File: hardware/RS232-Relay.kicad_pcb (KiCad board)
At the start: 2 copper layers, 82.5 x 151 mm, 204 parts, among them J1 Conn_01x08, J2 Conn_01x02, J3 Conn_01x08, J4 Conn_01x09, J5 Conn_01x09, J6 Conn_01x08, J7 RS232_1, J8 RS232_2, K1 G5V-1, K13 G5V-1, K14 G5V-1, K15 G5V-1, K2 G5V-1, K3 G5V-1, K4 G5V-1, K5 G5V-1, K6 G5V-1, K7 G5V-1, K8 G5V-1, K9 G5V-1, Q1 SS8050, Q10 SS8050, Q11 SS8050, Q12 SS8050, Q13 SS8050, Q14 SS8050, Q15 SS8050, Q16 SS8050, Q17 SS8050, Q18 SS8050, Q19 SS8050, Q2 SS8050, Q20 SS8050, Q21 SS8050, Q22 SS8050, Q23 SS8050, Q24 SS8050, Q3 SS8050, Q4 SS8050, Q5 SS8050, Q6 SS8050, Q7 SS8050, Q8 SS8050, Q9 SS8050, SW2 SW_SPST, SW3 SW_SPST, U1 TEC2-1210WI, U10 PC817, U11 PC817, U12 PC817, U13 PC817, U14 PC817, U15 PC817, U2 PC817, U3 PCF8575DBR, U4 MAX3232, U5 PC817, U6 PC817, U7 PC817, U8 PC817, U9 PC817

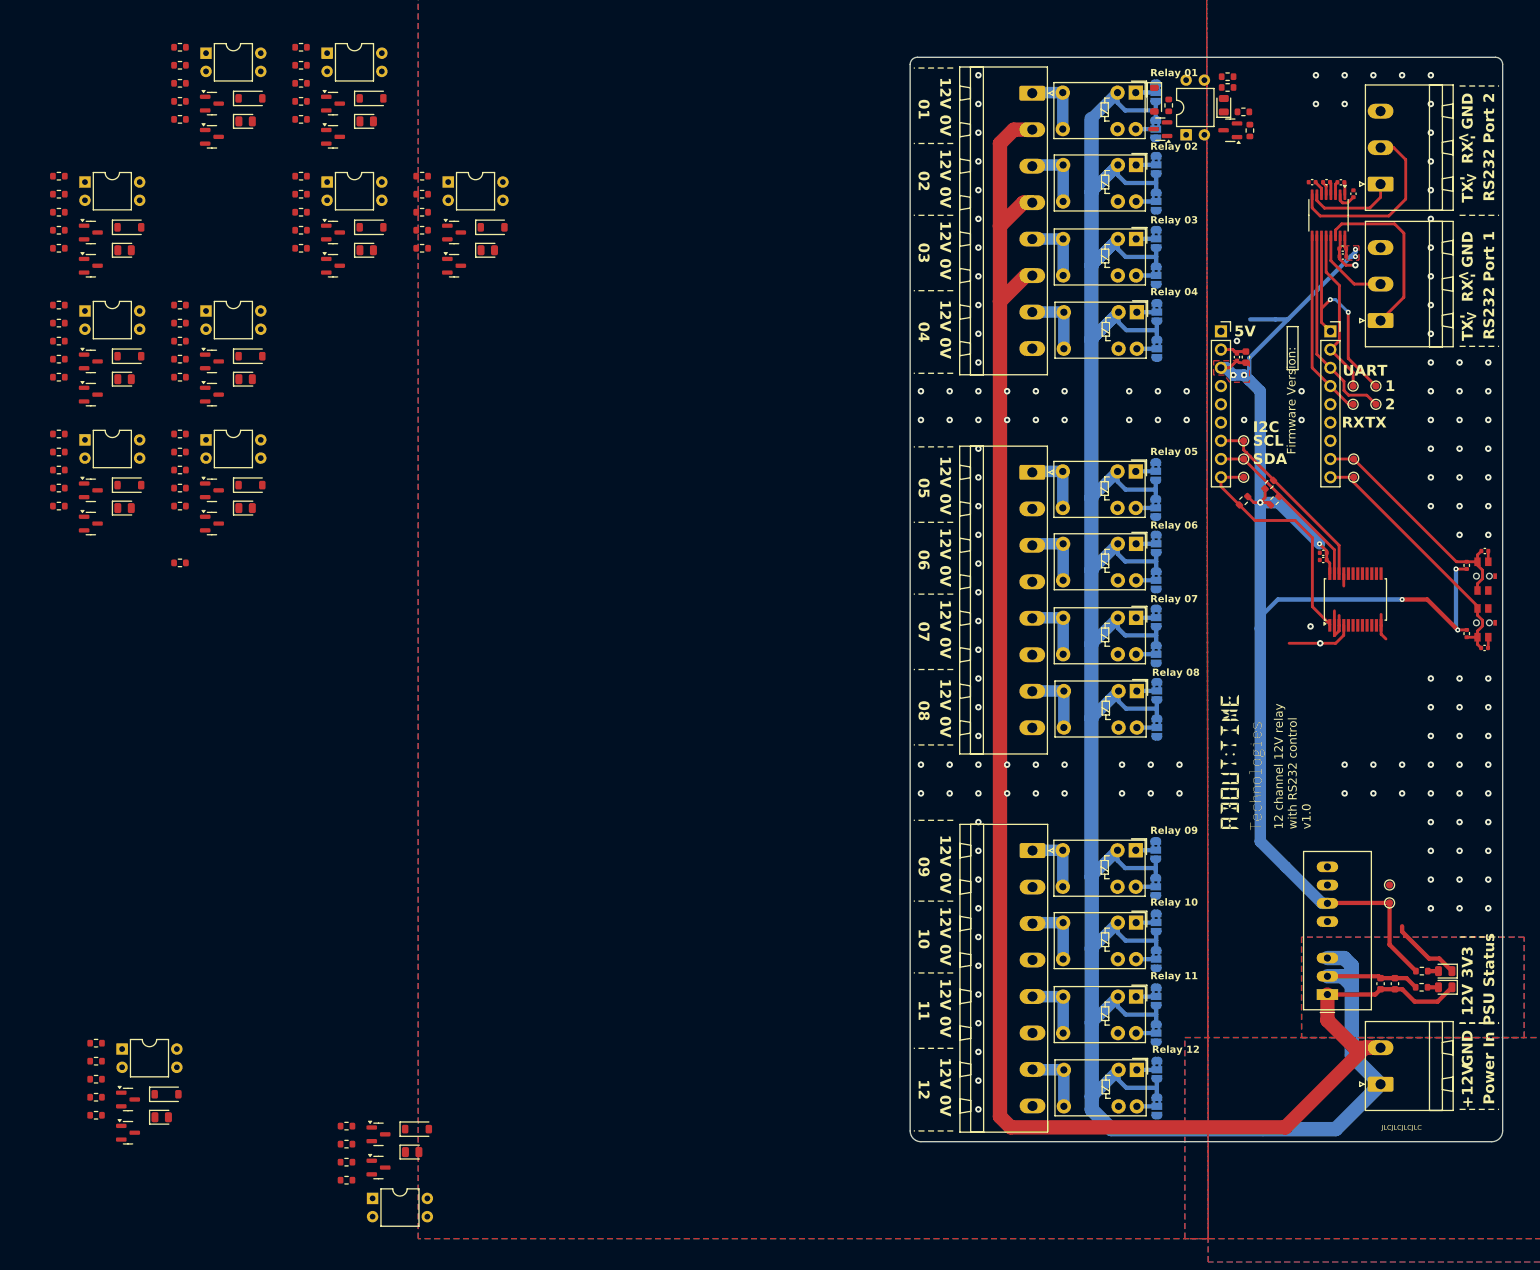
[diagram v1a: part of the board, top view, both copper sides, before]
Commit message: It could work but it's too big
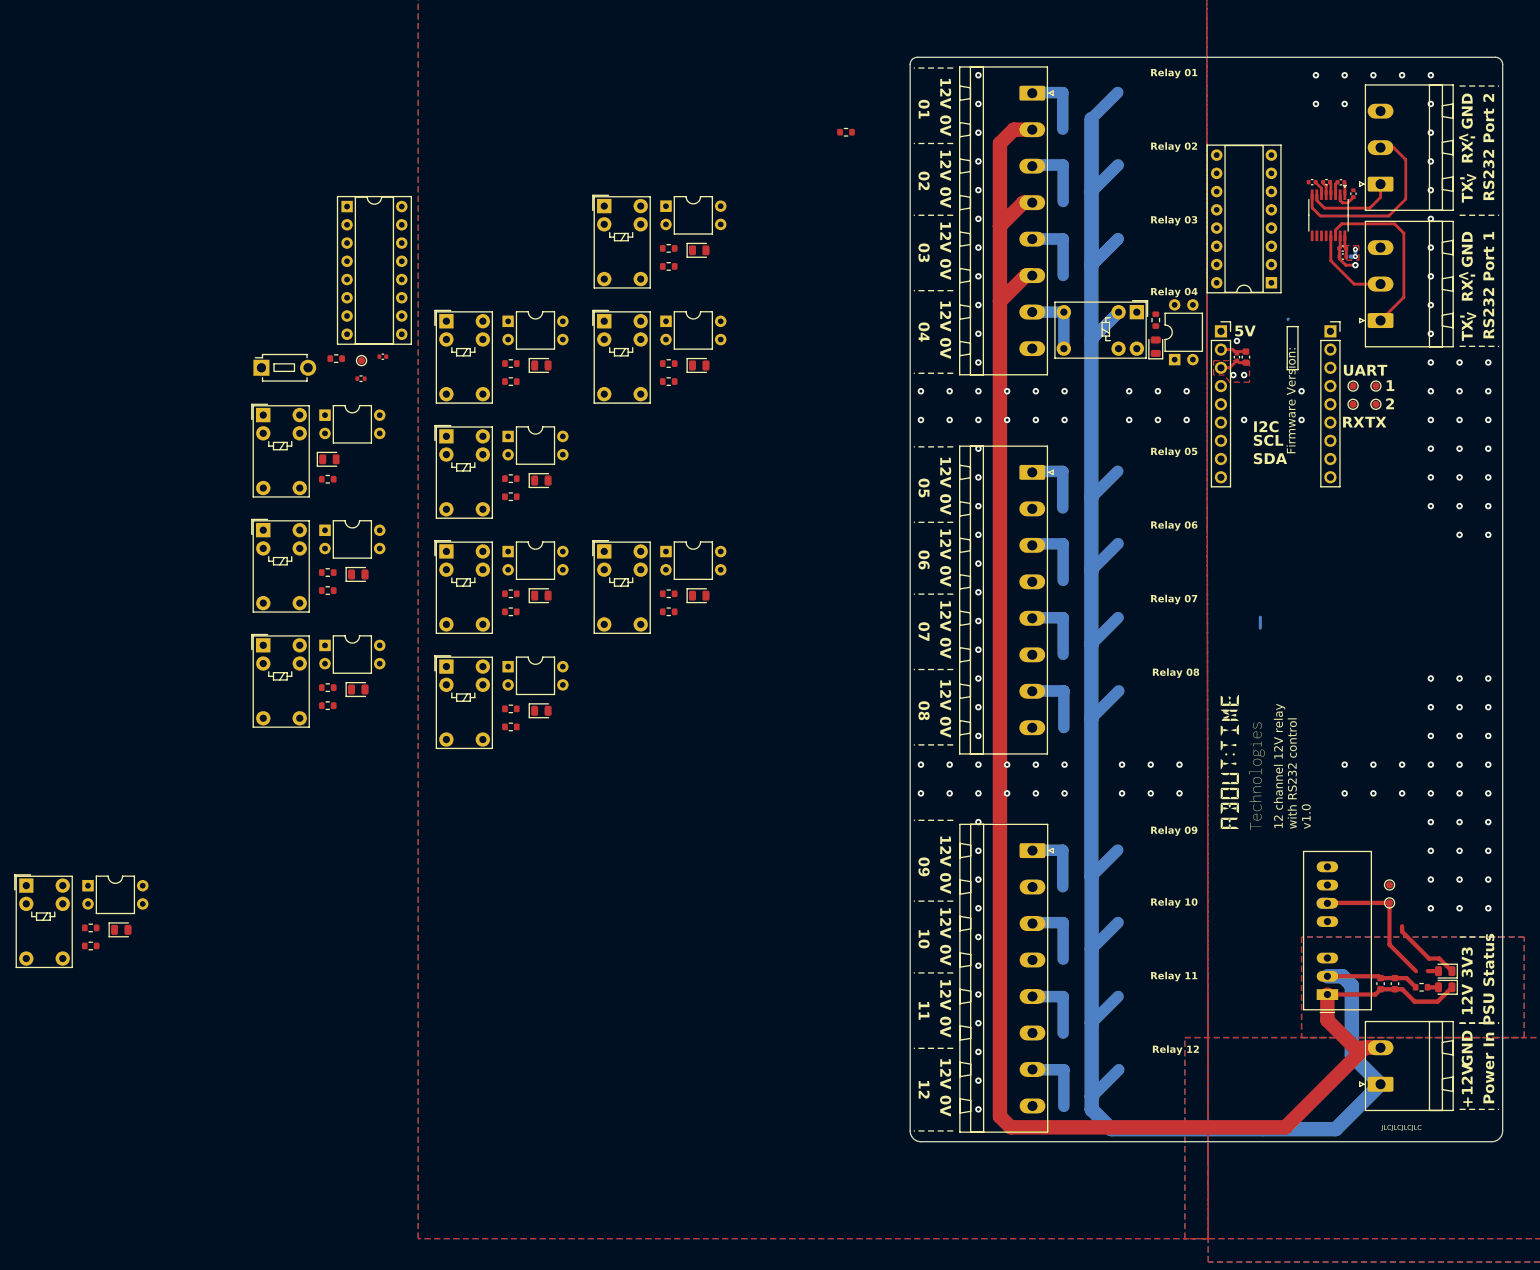
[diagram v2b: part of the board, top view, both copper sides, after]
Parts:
- removed C12, C15: 1uF, Capacitor_SMD:C_0402_1005Metric
- removed C13: 0.1uF, Capacitor_SMD:C_0402_1005Metric
- removed D15, D17, D19, D21, D29, D31, D33: 1N4148W, Diode_SMD:D_SOD-123
- removed D16, D18, D20, D22, D23: RED, LED_SMD:LED_0805_2012Metric
- removed JP1, JP10, JP11, JP12, JP2, JP3, JP4, JP49, JP5, JP50, JP51, JP52, JP53, JP54, JP55, JP56, JP57, JP58, JP59, JP6, JP60, JP7, JP8, JP9: Jumper_3_Bridged12, Jumper:SolderJumper-3_P1.3mm_Bridged2Bar12_RoundedPad1.0x1.5mm
- removed K13, K14, K15: G5V-1, Relay_THT:Relay_SPDT_Omron_G5V-1
- removed Q1, Q10, Q11, Q12, Q13, Q14, Q15, Q16, Q17, Q18, Q19, Q2, Q20, Q21, Q22, Q23, Q24, Q3, Q4, Q5, Q6, Q7, Q8, Q9: SS8050, Package_TO_SOT_SMD:SOT-23
- removed R10: 2000R, Resistor_SMD:R_0603_1608Metric
- removed R29, R30, R31, R32, R33, R34, R35, R36, R37, R38, R39, R40, R41, R42, R43, R44, R45, R46, R47, R48, R49, R50, R51, R52, R53, R54, R55: 4.7kR, Resistor_SMD:R_0603_1608Metric
- removed R56, R57, R58, R59, R60, R61, R62, R63, R64, R65, R66, R67: 100kR, Resistor_SMD:R_0603_1608Metric
- removed R7: 10K, Resistor_SMD:R_0402_1005Metric
- removed SW3: SW_SPST, Switch:PTS841
- removed TP10: I2C_SCL, TestPoint:TestPoint_Pad_D1.0mm
- removed TP11: I2C_INT, TestPoint:TestPoint_Pad_D1.0mm
- removed TP13: BTN_02, TestPoint:TestPoint_Pad_D1.0mm
- removed TP9: I2C_SDA, TestPoint:TestPoint_Pad_D1.0mm
- added K10: G5V-1, Relay_THT:Relay_SPDT_Omron_G5V-1, F.Cu at (3.92, 88.3)
- added K11: G5V-1, Relay_THT:Relay_SPDT_Omron_G5V-1, F.Cu at (3.92, 120.3)
- added K12: G5V-1, Relay_THT:Relay_SPDT_Omron_G5V-1, F.Cu at (100.1, 71.0)
- added U16: ULN2003, Package_DIP:DIP-16_W7.62mm_Socket, F.Cu at (-9.91, 56.3)
- D11, D13, D2, D4, D9: value 1N4148W -> RED; footprint Diode_SMD:D_SOD-123 -> LED_SMD:LED_0805_2012Metric
- J1, J3, J6: footprint Header:PhoenixContact_MSTBA_2,5_8-G-5,08_1x08_P5.08mm_Horizontal -> Connector_Phoenix_MSTB:PhoenixContact_MSTBA_2,5_8-G-5,08_1x08_P5.08mm_Horizontal
- R1: value 1000R -> 2000R
- R11, R15, R17, R21, R23, R3: value 2000R -> 220R
- R13, R19, R25, R27: value 4.7kR -> 220R
- R16, R22, R26, R28, R5: value 4.7kR -> 2000R
- R2: value 1000R -> 220R
- R4, R9: value 4K7 -> 220R
- R8: value 4K7 -> 2000R
- SW2: footprint Switch:PTS841 -> Button_Switch_THT:SW_PUSH_1P1T_6x3.5mm_H4.3_APEM_MJTP1243
- U3: value PCF8575DBR -> ULN2003; footprint Package_SO:SSOP-24_5.3x8.2mm_P0.65mm -> Package_DIP:DIP-16_W7.62mm_Socket
- moved SW2 172.5 mm to (-21.8, 78.7), turned to 0 degrees
- moved R27 157.1 mm to (59.6, 45.9)
- moved R6 156.1 mm to (-7.96, 80.3), turned to 0 degrees
- moved C14 155.8 mm to (-4.93, 77.2), turned to 0 degrees
- moved K5 155.3 mm to (-54.6, 150.8), turned to 0 degrees
- moved R28 153.7 mm to (102.7, 72.1), turned to -90 degrees
- moved D14 144.2 mm to (102.7, 75.8), turned to 90 degrees
- moved K8 143.0 mm to (-21.6, 101.3), turned to 0 degrees
- moved K2 140.6 mm to (-21.6, 85.3), turned to 0 degrees
- moved TP12 138.8 mm to (-7.89, 77.7)
- moved K1 138.7 mm to (-21.6, 117.4), turned to 0 degrees
- moved U15 135.0 mm to (105.3, 77.6), turned to 90 degrees
- moved R8 134.9 mm to (-12.6, 125.8), turned to 0 degrees
- moved R26 134.8 mm to (12.9, 128.7), turned to 0 degrees
- moved R4 134.1 mm to (-12.6, 123.3), turned to 0 degrees
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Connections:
- net /Relay-Module2/RELAY_OUT_03 renamed /RELAY_OUT_11
- D1 pad 1: Net-(D1-K) -> /ULN_RELAY_05
- D10 pad 1: Net-(D10-K) -> /ULN_RELAY_12
- D11 pad 1: +12V -> /ULN_RELAY_01
- D12 pad 1: Net-(D12-K) -> /ULN_RELAY_02
- D13 pad 1: +12V -> /ULN_RELAY_03
- D14 pad 1: Net-(D14-K) -> /ULN_RELAY_04
- D2 pad 1: +12V -> /ULN_RELAY_06
- D3 pad 1: Net-(D3-K) -> /ULN_RELAY_07
- D4 pad 1: +12V -> /ULN_RELAY_08
- D7 pad 1: Net-(D7-K) -> /ULN_RELAY_09
- D8 pad 1: Net-(D8-K) -> /ULN_RELAY_10
- D9 pad 1: +12V -> /ULN_RELAY_11
- J1 pad 1: /Relay-Module/RELAY_OUT_01 -> /RELAY_OUT_01
- J1 pad 2: GNDREF -> GND
- J1 pad 3: /Relay-Module/RELAY_OUT_02 -> /RELAY_OUT_02
- J1 pad 4: GNDREF -> GND
- J1 pad 5: /Relay-Module/RELAY_OUT_03 -> /RELAY_OUT_03
- J1 pad 6: GNDREF -> GND
- J1 pad 7: /Relay-Module/RELAY_OUT_04 -> /RELAY_OUT_04
- J1 pad 8: GNDREF -> GND
- J3 pad 1: /Relay-Module1/RELAY_OUT_01 -> /RELAY_OUT_05
- J3 pad 2: GNDREF -> GND
- J3 pad 3: /Relay-Module1/RELAY_OUT_02 -> /RELAY_OUT_06
- J3 pad 4: GNDREF -> GND
- J3 pad 5: /Relay-Module1/RELAY_OUT_03 -> /RELAY_OUT_07
- J3 pad 6: GNDREF -> GND
- J3 pad 7: /Relay-Module1/RELAY_OUT_04 -> /RELAY_OUT_08
- J3 pad 8: GNDREF -> GND
- J4 pad 7: I2C_SCL -> /ESP_32_GPIO_03
- J4 pad 8: I2C_SDA -> /ESP_32_GPIO_04
- J4 pad 9: I2C_INT -> /ESP_32_GPIO_05
- J5 pad 3: UART_2_TX -> BTN_01
- J5 pad 4: UART_2_RX -> /ESP_32_GPIO_15
- J5 pad 8: BTN_01 -> /ESP_32_GPIO_21
- J5 pad 9: BTN_02 -> /ESP_32_GPIO_22
- J6 pad 1: /Relay-Module2/RELAY_OUT_01 -> /RELAY_OUT_09
- J6 pad 2: GNDREF -> GND
- J6 pad 3: /Relay-Module2/RELAY_OUT_02 -> /RELAY_OUT_10
- J6 pad 4: GNDREF -> GND
- J6 pad 6: GNDREF -> GND
- J6 pad 7: /Relay-Module2/RELAY_OUT_04 -> /RELAY_OUT_12
- J6 pad 8: GNDREF -> GND
- K1 pad 1: /Relay-Module/Relay-NO-ISO1/RELAY_OFF -> GND
- K1 pad 10: /Relay-Module/Relay-NO-ISO1/RELAY_ON -> +12V
- K1 pad 5: /Relay-Module/RELAY_OUT_02 -> /RELAY_OUT_06
- K1 pad 6: /Relay-Module/RELAY_OUT_02 -> /RELAY_OUT_06
- K1 pad 9: Net-(D2-A) -> /ULN_RELAY_06
- K2 pad 1: /Relay-Module1/Relay-NO-ISO1/RELAY_OFF -> GND
- K2 pad 10: /Relay-Module1/Relay-NO-ISO1/RELAY_ON -> +12V
- K2 pad 5: /Relay-Module1/RELAY_OUT_02 -> /RELAY_OUT_07
- K2 pad 6: /Relay-Module1/RELAY_OUT_02 -> /RELAY_OUT_07
- K2 pad 9: Net-(D4-A) -> /ULN_RELAY_07
- K3 pad 1: /Relay-Module2/Relay-NO-ISO1/RELAY_OFF -> GND
- K3 pad 10: /Relay-Module2/Relay-NO-ISO1/RELAY_ON -> +12V
- K3 pad 5: /Relay-Module2/RELAY_OUT_02 -> /RELAY_OUT_08
- K3 pad 6: /Relay-Module2/RELAY_OUT_02 -> /RELAY_OUT_08
- K3 pad 9: Net-(D9-A) -> /ULN_RELAY_08
- K4 pad 1: /Relay-Module/Relay-NO-ISO2/RELAY_OFF -> GND
- K4 pad 10: /Relay-Module/Relay-NO-ISO2/RELAY_ON -> +12V
- K4 pad 5: /Relay-Module/RELAY_OUT_03 -> /RELAY_OUT_09
- K4 pad 6: /Relay-Module/RELAY_OUT_03 -> /RELAY_OUT_09
- K4 pad 9: Net-(D11-A) -> /ULN_RELAY_09
- K5 pad 1: /Relay-Module1/Relay-NO-ISO2/RELAY_OFF -> GND
- K5 pad 10: /Relay-Module1/Relay-NO-ISO2/RELAY_ON -> +12V
- K5 pad 5: /Relay-Module1/RELAY_OUT_03 -> /RELAY_OUT_10
- K5 pad 6: /Relay-Module1/RELAY_OUT_03 -> /RELAY_OUT_10
- K5 pad 9: Net-(D13-A) -> /ULN_RELAY_10
- K6 pad 1: /Relay-Module2/Relay-NO-ISO2/RELAY_OFF -> GND
- K6 pad 10: /Relay-Module2/Relay-NO-ISO2/RELAY_ON -> +12V
- K6 pad 9: Net-(D15-A) -> /ULN_RELAY_11
- K7 pad 1: /Relay-Module/Relay-NO-ISO3/RELAY_OFF -> GND
- K7 pad 10: /Relay-Module/Relay-NO-ISO3/RELAY_ON -> +12V
- K7 pad 5: /Relay-Module/RELAY_OUT_04 -> /RELAY_OUT_12
- K7 pad 6: /Relay-Module/RELAY_OUT_04 -> /RELAY_OUT_12
- K7 pad 9: Net-(D17-A) -> /ULN_RELAY_12
- K8 pad 1: /Relay-Module1/Relay-NO-ISO3/RELAY_OFF -> GND
- K8 pad 10: /Relay-Module1/Relay-NO-ISO3/RELAY_ON -> +12V
- K8 pad 5: /Relay-Module1/RELAY_OUT_04 -> /RELAY_OUT_01
- K8 pad 6: /Relay-Module1/RELAY_OUT_04 -> /RELAY_OUT_01
- K8 pad 9: Net-(D19-A) -> /ULN_RELAY_01
- K9 pad 1: /Relay-Module2/Relay-NO-ISO3/RELAY_OFF -> GND
- K9 pad 10: /Relay-Module2/Relay-NO-ISO3/RELAY_ON -> +12V
- K9 pad 5: /Relay-Module2/RELAY_OUT_04 -> /RELAY_OUT_02
- K9 pad 6: /Relay-Module2/RELAY_OUT_04 -> /RELAY_OUT_02
- K9 pad 9: Net-(D21-A) -> /ULN_RELAY_02
- R11 pad 1: +3V3 -> /RELAY_IN_08
- R11 pad 2: Net-(D7-A) -> Net-(R11-Pad2)
- R12 pad 1: +3V3 -> +12V
- R12 pad 2: Net-(D8-A) -> Net-(D4-A)
- R13 pad 1: Net-(R13-Pad1) -> /RELAY_IN_09
- R13 pad 2: Net-(Q11-B) -> Net-(R13-Pad2)
- R14 pad 1: +3V3 -> +12V
- R14 pad 2: Net-(D10-A) -> Net-(D7-A)
- R15 pad 1: +3V3 -> /RELAY_IN_10
- R15 pad 2: Net-(D12-A) -> Net-(R15-Pad2)
- R16 pad 1: Net-(R16-Pad1) -> +12V
- R16 pad 2: Net-(Q12-B) -> Net-(D8-A)
- R17 pad 1: +3V3 -> /RELAY_IN_11
- R17 pad 2: Net-(D14-A) -> Net-(R17-Pad2)
- R18 pad 1: +3V3 -> +12V
- R18 pad 2: Net-(D16-A) -> Net-(D9-A)
- R19 pad 1: Net-(R19-Pad1) -> /RELAY_IN_12
- R19 pad 2: Net-(Q16-B) -> Net-(R19-Pad2)
- R20 pad 1: +3V3 -> +12V
- R20 pad 2: Net-(D18-A) -> Net-(D10-A)
- R21 pad 1: +3V3 -> /RELAY_IN_01
- R21 pad 2: Net-(D20-A) -> Net-(R21-Pad2)
- R22 pad 1: Net-(R22-Pad1) -> +12V
- R22 pad 2: Net-(Q17-B) -> Net-(D11-A)
- R23 pad 1: +3V3 -> /RELAY_IN_02
- R23 pad 2: Net-(D22-A) -> Net-(R23-Pad2)
- R24 pad 1: +3V3 -> +12V
- R24 pad 2: Net-(D23-A) -> Net-(D12-A)
- R25 pad 1: Net-(R25-Pad1) -> /RELAY_IN_03
- R25 pad 2: Net-(Q18-B) -> Net-(R25-Pad2)
- R26 pad 1: +3V3 -> +12V
- R26 pad 2: Net-(R26-Pad2) -> Net-(D13-A)
- R27 pad 1: +3V3 -> /RELAY_IN_04
- R28 pad 1: Net-(R28-Pad1) -> +12V
- R28 pad 2: Net-(Q19-B) -> Net-(D14-A)
- R3 pad 1: +3V3 -> /RELAY_IN_05
- R3 pad 2: Net-(D1-A) -> Net-(R3-Pad2)
- R4 pad 1: I2C_SCL -> /RELAY_IN_06
- R4 pad 2: +3V3 -> Net-(R4-Pad2)
- R5 pad 1: Net-(R5-Pad1) -> +12V
- R5 pad 2: Net-(Q10-B) -> Net-(D1-A)
- R8 pad 1: +3V3 -> +12V
- R8 pad 2: I2C_SDA -> Net-(D2-A)
- R9 pad 1: I2C_INT -> /RELAY_IN_07
- R9 pad 2: +3V3 -> Net-(R9-Pad2)
- U1 pad 3: +12V -> GND
- U10 pad 1: Net-(R35-Pad2) -> Net-(R17-Pad2)
- U10 pad 2: Net-(D14-K) -> GNDREF
- U10 pad 3: Net-(R28-Pad1) -> /ULN_ISO_11
- U11 pad 1: Net-(R36-Pad2) -> Net-(R19-Pad2)
- U11 pad 2: Net-(D16-K) -> GNDREF
- U11 pad 3: Net-(R31-Pad1) -> /ULN_ISO_12
- U12 pad 1: Net-(R37-Pad2) -> Net-(R21-Pad2)
- U12 pad 2: Net-(D18-K) -> GNDREF
- U12 pad 3: Net-(R34-Pad1) -> /ULN_ISO_01
- U13 pad 1: Net-(R38-Pad2) -> Net-(R23-Pad2)
- U13 pad 2: Net-(D20-K) -> GNDREF
- U13 pad 3: Net-(R46-Pad1) -> /ULN_ISO_02
- U14 pad 1: Net-(R39-Pad2) -> Net-(R25-Pad2)
- U14 pad 2: Net-(D22-K) -> GNDREF
- U14 pad 3: Net-(R49-Pad1) -> /ULN_ISO_03
- U15 pad 1: Net-(R40-Pad2) -> Net-(R27-Pad2)
- U15 pad 2: Net-(D23-K) -> GNDREF
- U15 pad 3: Net-(R52-Pad1) -> /ULN_ISO_04
- U2 pad 1: Net-(R26-Pad2) -> Net-(R3-Pad2)
- U2 pad 2: Net-(D1-K) -> GNDREF
- U2 pad 3: Net-(R5-Pad1) -> /ULN_ISO_05
- U3 pad 1: I2C_INT -> /ULN_ISO_01
- U3 pad 10: RELAY_IN_06 -> unconnected-(U3-O7-Pad10)
- U3 pad 11: RELAY_IN_05 -> /ULN_RELAY_06
- U3 pad 12: GNDREF -> /ULN_RELAY_05
- U3 pad 13: RELAY_IN_04 -> /ULN_RELAY_04
- U3 pad 14: RELAY_IN_03 -> /ULN_RELAY_03
- U3 pad 15: RELAY_IN_02 -> /ULN_RELAY_02
- U3 pad 16: RELAY_IN_01 -> /ULN_RELAY_01
- U3 pad 2: GNDREF -> /ULN_ISO_02
- U3 pad 3: GNDREF -> /ULN_ISO_03
- U3 pad 4: RELAY_IN_12 -> /ULN_ISO_04
- U3 pad 5: RELAY_IN_11 -> /ULN_ISO_05
- U3 pad 6: RELAY_IN_10 -> /ULN_ISO_06
- U3 pad 7: RELAY_IN_09 -> unconnected-(U3-I7-Pad7)
- U3 pad 8: RELAY_IN_08 -> GND
- U3 pad 9: RELAY_IN_07 -> +12V
- U5 pad 1: Net-(R27-Pad2) -> Net-(R4-Pad2)
- U5 pad 2: Net-(D3-K) -> GNDREF
- U5 pad 3: Net-(R13-Pad1) -> /ULN_ISO_06
- U6 pad 1: Net-(R29-Pad2) -> Net-(R9-Pad2)
- U6 pad 2: Net-(D7-K) -> GNDREF
- U6 pad 3: Net-(R16-Pad1) -> /ULN_ISO_07
- U7 pad 1: Net-(R30-Pad2) -> Net-(R11-Pad2)
- U7 pad 2: Net-(D8-K) -> GNDREF
- U7 pad 3: Net-(R19-Pad1) -> /ULN_ISO_08
- U8 pad 1: Net-(R32-Pad2) -> Net-(R13-Pad2)
- U8 pad 2: Net-(D10-K) -> GNDREF
- U8 pad 3: Net-(R22-Pad1) -> /ULN_ISO_09
- U9 pad 1: Net-(R33-Pad2) -> Net-(R15-Pad2)
- U9 pad 2: Net-(D12-K) -> GNDREF
- U9 pad 3: Net-(R25-Pad1) -> /ULN_ISO_10
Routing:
- net +3V3: track 203.8 -> 30.1 mm, vias 9 -> 4
- net +12V: track 414.7 -> 291.7 mm
- net BTN_02: track 36.4 -> 0.00 mm
- net I2C_INT: track 33.3 -> 0.00 mm
- net BTN_01: track 32.7 -> 0.00 mm
- net UART_1_TX: track 30.7 -> 0.00 mm, vias 2 -> 0
- net UART_2_TX: track 28.4 -> 0.00 mm
- net I2C_SCL: track 27.2 -> 0.00 mm
- net UART_2_RX: track 26.2 -> 0.00 mm
- net I2C_SDA: track 24.4 -> 0.00 mm
- net UART_1_RX: track 23.5 -> 0.00 mm
- net GNDREF: track 35.0 -> 20.0 mm, vias 75 -> 74
- net /Relay-Module1/RELAY_OUT_04: track 9.49 -> 0.00 mm
- net /RELAY_OUT_08: track 0.00 -> 9.49 mm
- net /Relay-Module2/RELAY_OUT_04: track 9.49 -> 0.00 mm
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
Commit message: Schematic ready
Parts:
- removed R27: 220R, Resistor_SMD:R_0603_1608Metric
- removed U10, U11, U12, U13, U14, U15, U7, U8, U9: PC817, Package_DIP:DIP-4_W7.62mm
- added R10: 2000R, Resistor_SMD:R_0603_1608Metric, F.Cu at (103.0, 118.2)
- added R7: 220R, Resistor_SMD:R_0603_1608Metric, F.Cu at (123.8, 105.5)
- U16, U3: footprint Package_DIP:DIP-16_W7.62mm_Socket -> Package_DIP:DIP-16_W7.62mm_SMDSocket_SmallPads
- U2, U5, U6: value PC817 -> LTV-847; footprint Package_DIP:DIP-4_W7.62mm -> Package_DIP:DIP-16_W7.62mm_SMDSocket_SmallPads
- moved R15 175.6 mm to (123.8, 110.5)
- moved SW2 173.8 mm to (148.3, 114.2), turned to 90 degrees
- moved R2 173.6 mm to (139.7, 162.8)
- moved TP12 157.0 mm to (144.5, 115.5)
- moved R6 155.0 mm to (143.8, 112.0)
- moved K5 154.6 mm to (100.0, 156.0), turned to -90 degrees
- moved R4 153.8 mm to (117.7, 41.5)
- moved C14 152.0 mm to (143.6, 109.5)
- moved R16 148.6 mm to (103.0, 160.7), turned to 90 degrees
- moved U6 147.5 mm to (112.0, 163.7), turned to 180 degrees
- moved D8 144.4 mm to (103.0, 157.0), turned to -90 degrees
- moved K7 141.8 mm to (100.1, 176.5), turned to -90 degrees
- moved U5 141.1 mm to (115.0, 58.0), turned to 180 degrees
- moved R9 139.6 mm to (117.7, 44.0)
- moved K8 136.0 mm to (100.0, 40.4), turned to -90 degrees
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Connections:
- R11 pad 1: /RELAY_IN_08 -> /RELAY_IN_04
- R13 pad 1: /RELAY_IN_09 -> /RELAY_IN_06
- R15 pad 1: /RELAY_IN_10 -> /RELAY_IN_07
- R17 pad 1: /RELAY_IN_11 -> /RELAY_IN_08
- R19 pad 1: /RELAY_IN_12 -> /RELAY_IN_09
- R21 pad 1: /RELAY_IN_01 -> /RELAY_IN_10
- R23 pad 1: /RELAY_IN_02 -> /RELAY_IN_11
- R25 pad 1: /RELAY_IN_03 -> /RELAY_IN_12
- R3 pad 1: /RELAY_IN_05 -> /RELAY_IN_01
- R4 pad 1: /RELAY_IN_06 -> /RELAY_IN_02
- R9 pad 1: /RELAY_IN_07 -> /RELAY_IN_03
- U2 pad 1: Net-(R3-Pad2) -> Net-(R7-Pad2)
- U2 pad 3: /ULN_ISO_05 -> Net-(R13-Pad2)
- U2 pad 4: +12V -> GNDREF
- U5 pad 1: Net-(R4-Pad2) -> Net-(R3-Pad2)
- U5 pad 3: /ULN_ISO_06 -> Net-(R4-Pad2)
- U5 pad 4: +12V -> GNDREF
- U6 pad 1: Net-(R9-Pad2) -> Net-(R19-Pad2)
- U6 pad 3: /ULN_ISO_07 -> Net-(R21-Pad2)
- U6 pad 4: +12V -> GNDREF
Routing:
- net +12V: track 291.7 -> 403.2 mm
- net /ULN_RELAY_12: track 0.00 -> 51.1 mm
- net /ULN_RELAY_01: track 0.00 -> 46.3 mm
- net /ULN_RELAY_11: track 0.00 -> 41.1 mm
- net /ULN_RELAY_02: track 0.00 -> 35.1 mm
- net /ULN_RELAY_10: track 0.00 -> 32.1 mm
- net UART_1_RX: track 0.00 -> 24.2 mm
- net UART_1_TX: track 0.00 -> 24.1 mm, vias 0 -> 1
- net /ULN_RELAY_03: track 0.00 -> 23.8 mm
- net /ULN_RELAY_09: track 0.00 -> 12.5 mm
- net /ULN_RELAY_04: track 0.00 -> 12.4 mm
- net /ULN_RELAY_05: track 0.00 -> 7.73 mm
- net /ULN_RELAY_07: track 0.00 -> 7.70 mm
- net /ULN_RELAY_08: track 0.00 -> 7.68 mm
- net /ULN_RELAY_06: track 0.00 -> 7.60 mm
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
